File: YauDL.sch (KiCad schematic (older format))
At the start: 41 parts, among them K1 HEATSINK, Q1 IRL3803, Q2 IRL3803, Q3 AO3401, Q4 AO3401, SW1 SWITCH_INV, T1 Binding post, T2 Binding post, T3 Binding post, T4 Binding post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

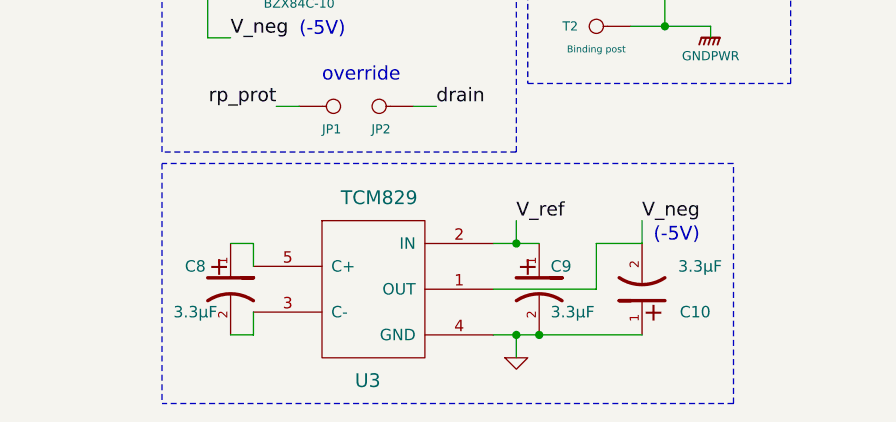
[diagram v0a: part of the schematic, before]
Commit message: Revert "Tweaks..."
This reverts commit 0c1dc09ceebd5a01f0e86e24f0b4b3829b1a22fd.
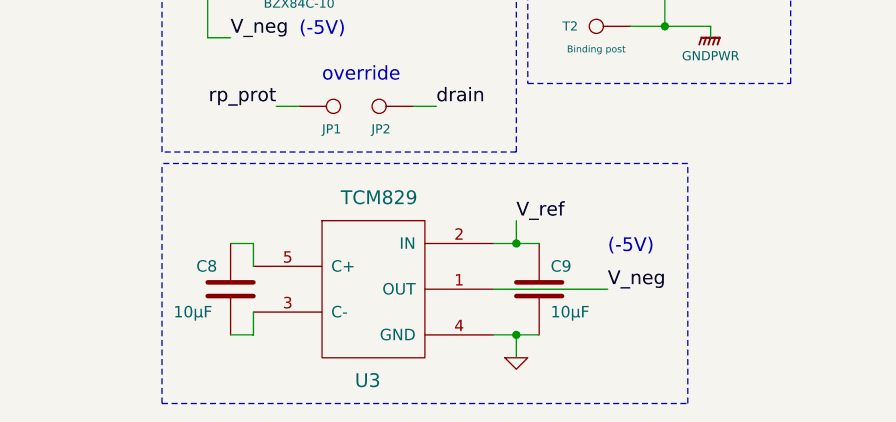
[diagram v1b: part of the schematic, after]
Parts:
- removed C10, C8, C9: 3.3µF, symbol CP1
- added C8, C9: 10µF, symbol C
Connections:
- net GND: now also C9.2
- net V_ref: now also C9.1
- net at U3.3 (C-): now also C8.2
- net at U3.5 (C+): now also C8.1

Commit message: Tweaks...
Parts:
- removed C8, C9: 10µF, symbol C
- added C10, C8, C9: 3.3µF, symbol CP1
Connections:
- net GND: now also C10.1, C9.2
- net V_neg: now also C10.2
- net V_ref: now also C9.1
- net at U3.3 (C-): now also C8.2
- net at U3.5 (C+): now also C8.1
